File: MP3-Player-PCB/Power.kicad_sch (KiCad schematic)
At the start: 3 parts, among them J301 Conn_01x02_Socket, U301 BQ24259, U302 TLV73333PDBV

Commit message: Started power schematic
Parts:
- added C201, C202: 100n, symbol Device:C
- added C203, C204, C206, C207, C208, C209: 10u, symbol Device:C
- added C205: 47n, symbol Device:C
- added J202: USB_C_Receptacle_USB2.0_16P, symbol Connector:USB_C_Receptacle_USB2.0_16P
- added L201: L, symbol Device:L
- added R201: 0R, symbol Device:R
- added R202, R203: 5.1k, symbol Device:R
- added R204: R, symbol Device:R
- added U203: TLV73333PDBV, Package_TO_SOT_SMD:SOT-23-5, symbol Regulator_Linear:TLV73333PDBV
- added U204: USBLC6-2SC6, Package_TO_SOT_SMD:SOT-23-6, symbol Power_Protection:USBLC6-2SC6
- renumbered J301 to J201, U301 to U201, U302 to U202
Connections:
- net +VUSB_FILT: now reaches U201.1 (VBUS)
- net +VUSB_FILT: now also U201.24 (VBUS), C201.1, C203.1, R201.2
- net at U201.10 (ILIM): now also R204.1
- net GND: now reaches U201.17 (PGND)
- net GND: now also U201.18 (PGND), C201.2, C202.2, C203.2, C204.2, C206.2, C207.2, C208.2, C209.2, J202.A1 (GND), J202.A12 (GND), J202.B1 (GND), J202.B12 (GND), J202.S1 (SHIELD), R202.2, R203.2, R204.2
- net at U201.19 (SW): now also U201.20 (SW), C205.2, L201.1
- net at U201.21 (BTST): now also C205.1
- net at U201.23 (PMID): now also C204.1
- new net +VSYS: C206.1, C207.1, C208.1, C209.1, L201.2
- new net +VUSB: C202.1, J202.A4 (VBUS), J202.A9 (VBUS), J202.B4 (VBUS), J202.B9 (VBUS), R201.1
- new net USB_CON_CC1: J202.A5 (CC1), R202.1
- new net USB_CON_CC2: J202.B5 (CC2), R203.1
- new net USB_CON_D+: J202.A6 (D+), J202.B6 (D+), U204.3 (I/O2)
- new net USB_CON_D-: J202.A7 (D-), J202.B7 (D-), U204.1 (I/O1)
- new net USB_MCU_D+: U204.4 (I/O2)
- new net USB_MCU_D-: U204.6 (I/O1)
- no-connect marks 0 -> 2
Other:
- moved on the sheet: J201, U201, U202

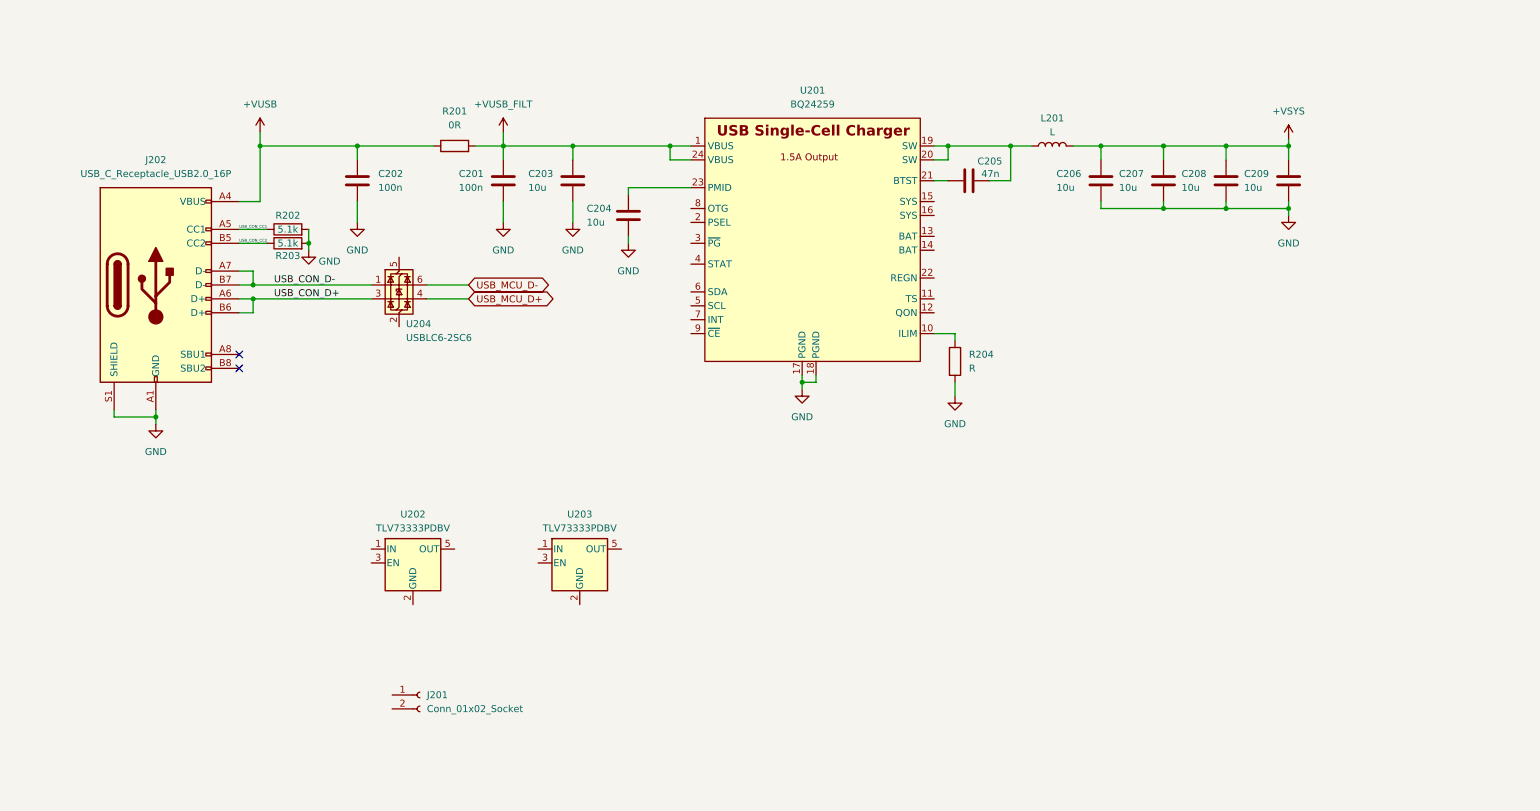
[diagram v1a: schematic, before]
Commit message: Adding i2c connections to charger ic as well as ntc safety logic
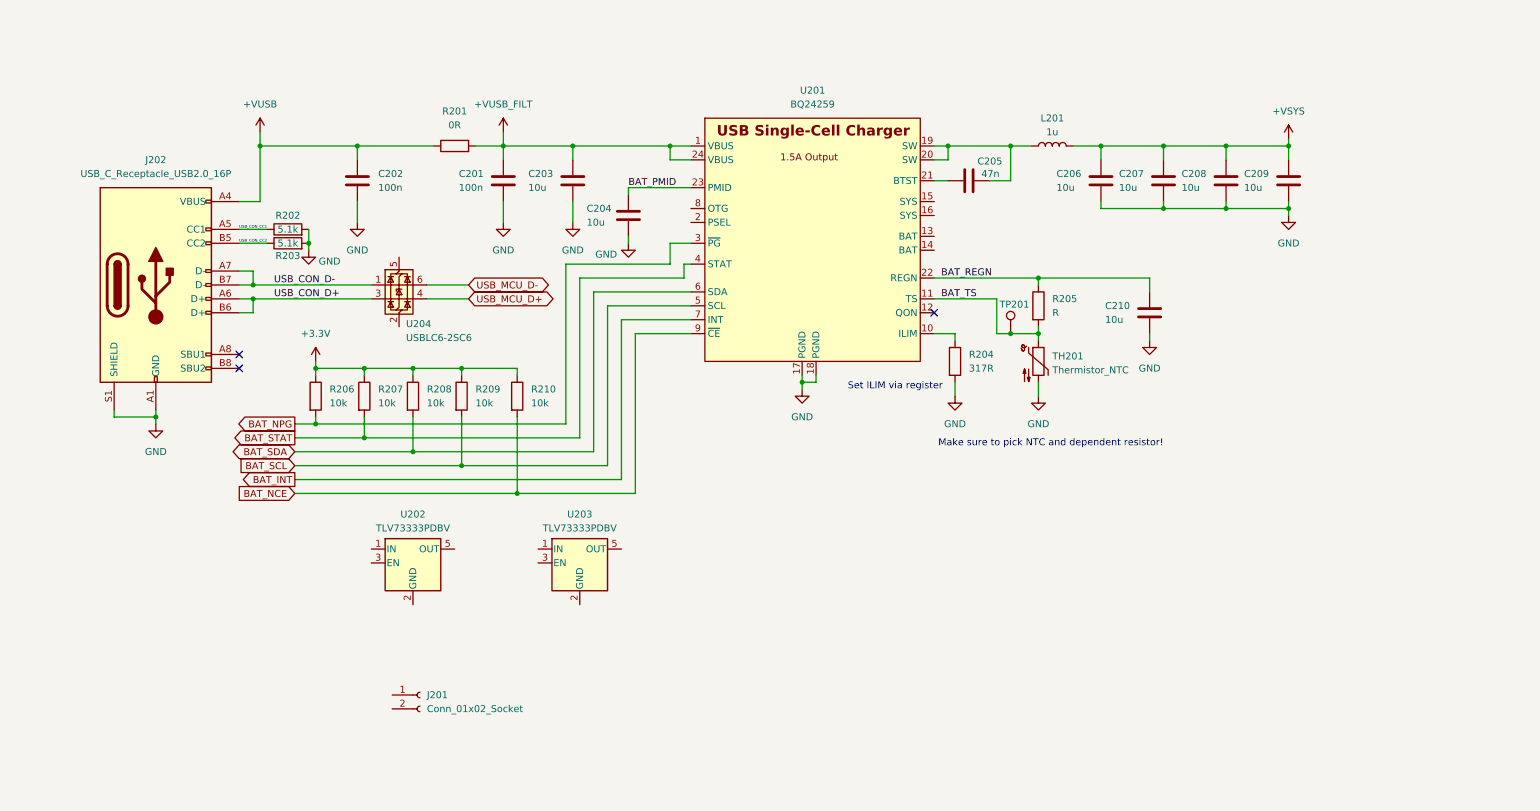
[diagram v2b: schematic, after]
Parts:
- added C210: 10u, symbol Device:C
- added R205: R, symbol Device:R
- added R206, R207, R208, R209, R210: 10k, symbol Device:R
- added TH201: Thermistor_NTC, symbol Device:Thermistor_NTC
- added TP201: TestPoint, symbol Connector:TestPoint
- L201: value L -> 1u
- R204: value R -> 317R
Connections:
- net GND: now also C210.2, TH201.2
- net BAT_PMID: now reaches C204.1, U201.23 (PMID)
- net BAT_TS: now reaches U201.11 (TS)
- net BAT_TS: now also R205.2, TH201.1, TP201.1
- net BAT_REGN: now reaches U201.22 (REGN)
- net BAT_REGN: now also C210.1, R205.1
- net BAT_NPG: now reaches U201.3 (~{PG})
- net BAT_NPG: now also R206.2
- net BAT_STAT: now reaches U201.4 (STAT)
- net BAT_STAT: now also R207.2
- net BAT_SCL: now reaches U201.5 (SCL)
- net BAT_SCL: now also R209.2
- net BAT_SDA: now reaches U201.6 (SDA)
- net BAT_SDA: now also R208.2
- net BAT_INT: now reaches U201.7 (INT)
- net BAT_NCE: now reaches U201.9 (~{CE})
- net BAT_NCE: now also R210.2
- new net +3.3V: R206.1, R207.1, R208.1, R209.1, R210.1
- no-connect marks 2 -> 3
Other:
- note added: "Make sure to pick NTC and dependent resistor!"
- note added: "Set ILIM via register"

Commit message: Added charger IC schematic circuitry
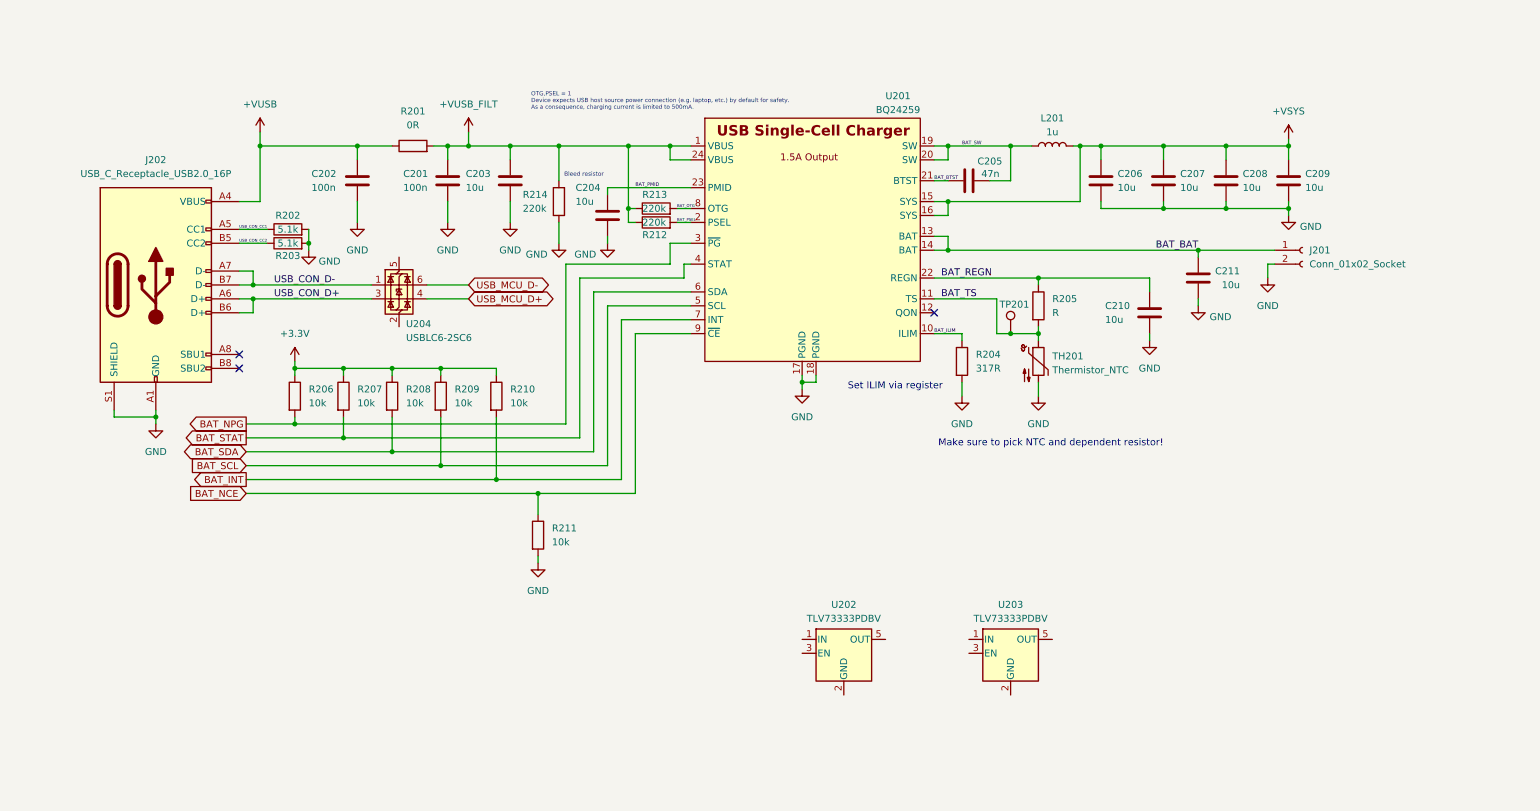
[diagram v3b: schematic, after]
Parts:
- added C211: 10u, symbol Device:C
- added R211: 10k, symbol Device:R
- added R212, R213, R214: 220k, symbol Device:R
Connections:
- net +VSYS: now also U201.15 (SYS), U201.16 (SYS)
- net +VUSB_FILT: now also R212.1, R213.1, R214.2
- net BAT_INT: now also R210.2
- net BAT_NCE: now also R211.1; no longer R210.2
- net GND: now also J201.2 (Pin_2), C211.2, R211.2, R214.1
- net BAT_BAT: now reaches J201.1 (Pin_1)
- net BAT_BAT: now also U201.13 (BAT), U201.14 (BAT), C211.1
- net BAT_ILIM: now reaches R204.1, U201.10 (ILIM)
- net BAT_SW: now reaches C205.2, L201.1, U201.19 (SW), U201.20 (SW)
- net BAT_PSEL: now reaches U201.2 (PSEL)
- net BAT_PSEL: now also R212.2
- net BAT_BTST: now reaches C205.1, U201.21 (BTST)
- net BAT_OTG: now reaches U201.8 (OTG)
- net BAT_OTG: now also R213.2
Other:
- note added: "Bleed resistor"
- note added: "OTG,PSEL = 1 Device expects USB host source power connection (e.g. laptop, etc.) by default for safety. As a consequence, charging current is limited to 500mA."
- moved on the sheet: C201, C203, C204, J201, R201, R204, R206, R207, R208, R209, R210, U202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

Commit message: Added new LDO (TPS7A20) schematic symbol and wired it up on power page for both analog and digital supplies
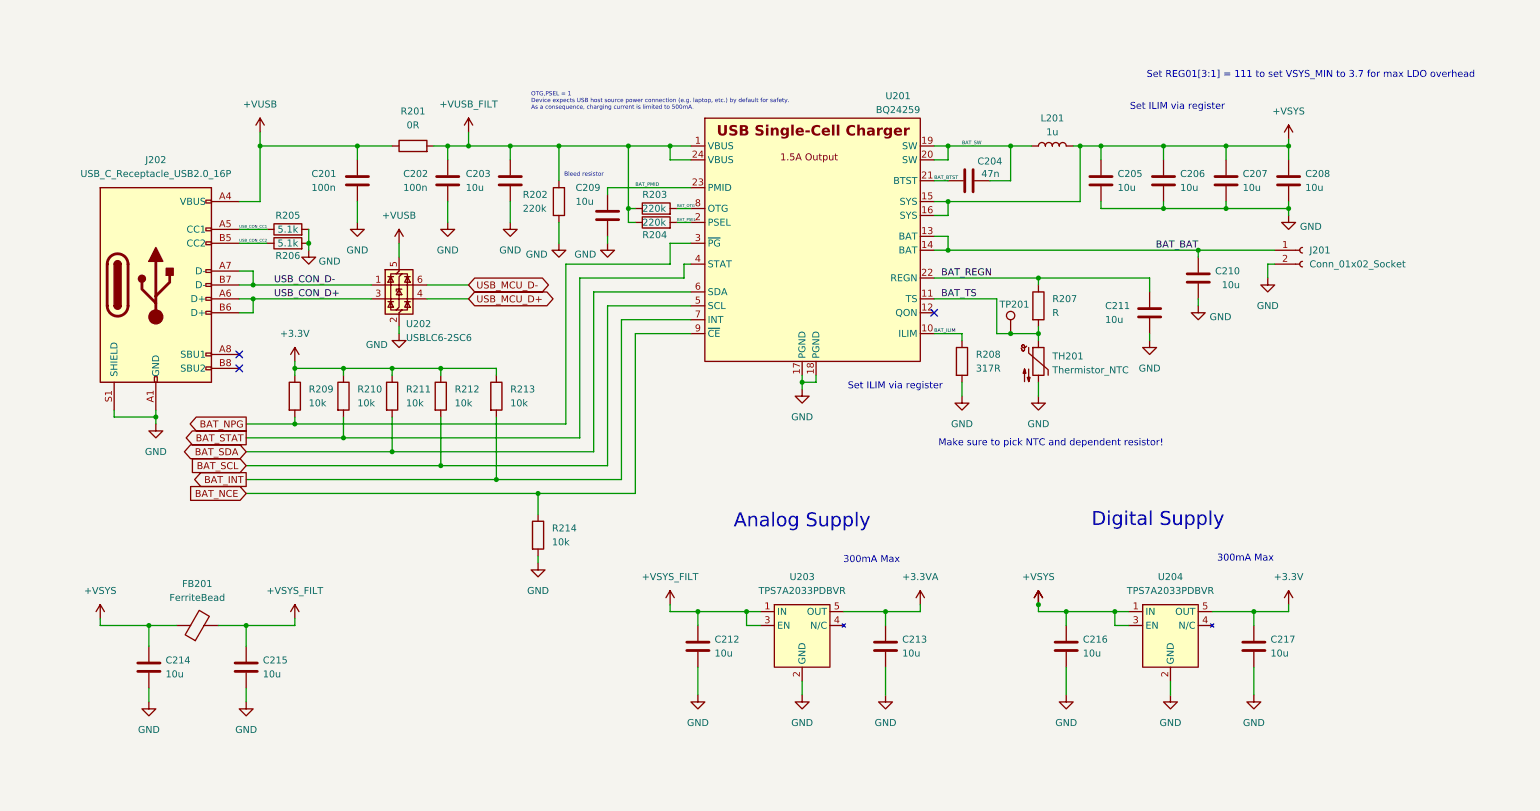
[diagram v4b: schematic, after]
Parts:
- removed U202, U203: TLV73333PDBV, Package_TO_SOT_SMD:SOT-23-5, symbol Regulator_Linear:TLV73333PDBV
- added C212, C213, C214, C215, C216, C217: 10u, symbol Device:C
- added FB201: FerriteBead, symbol Device:FerriteBead
- added U203, U204: TPS7A2033PDBVR, symbol MP3-Player_Symbol_Libraries:TPS7A2033PDBVR
- renumbered C202 to C201, C201 to C202, C205 to C204, C206 to C205, C207 to C206, C208 to C207, C209 to C208, C204 to C209, C211 to C210, C210 to C211, R214 to R202, R213 to R203, R212 to R204, R202 to R205, R203 to R206, R205 to R207, R204 to R208, R206 to R209, R207 to R210, R208 to R211, R209 to R212, R210 to R213, R211 to R214, U204 to U202
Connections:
- net +3.3V: now also C217.1, U204.5 (OUT)
- net +VSYS: now also C212.1, C214.1, C215.1, C216.1, FB201.1, FB201.2, U203.1 (IN), U203.3 (EN), U204.1 (IN), U204.3 (EN)
- net +VUSB: now also U202.5 (VBUS)
- net GND: now also U202.2 (GND), C212.2, C213.2, C214.2, C215.2, C216.2, C217.2, U203.2 (GND), U204.2 (GND)
- new net +3.3VA: C213.1, U203.5 (OUT)
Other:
- note added: "300mA Max"
- note added: "Analog Supply"
- note added: "Digital Supply"
- note added: "Set REG01[3:1] = 111 to set VSYS_MIN to 3.7 for max LDO overhead"

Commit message: Added addressable LED circuitry
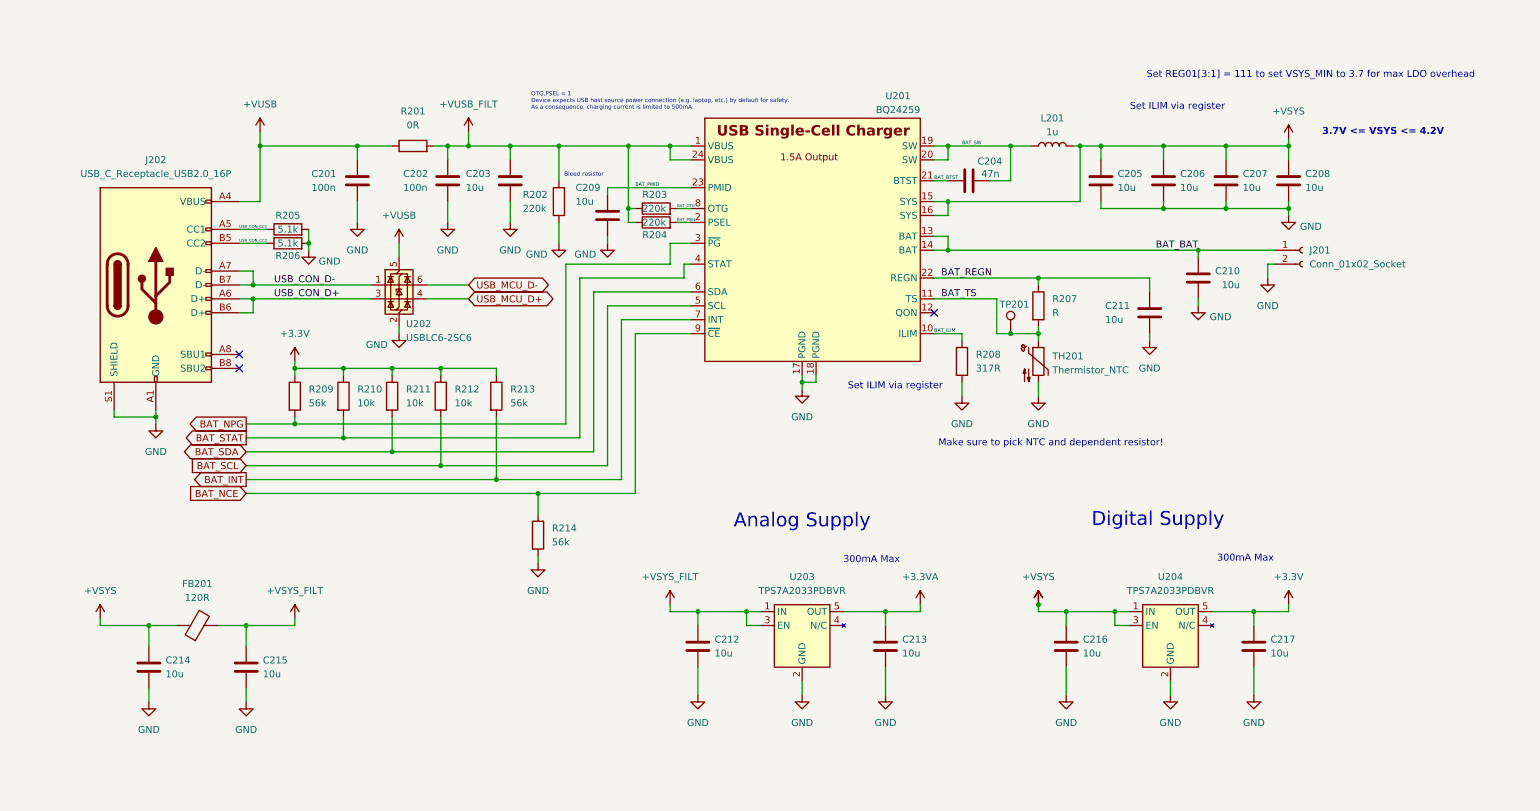
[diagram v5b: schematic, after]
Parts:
- FB201: value FerriteBead -> 120R
- R209, R213, R214: value 10k -> 56k
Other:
- note added: "3.7V <= VSYS <= 4.2V"
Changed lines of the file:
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@@
 		)
 	)
+	(text "3.7V <= VSYS <= 4.2V"
+		(exclude_from_sim no)
+		(at 263.652 38.1 0)
+		(effects
+			(font
+				(size 1.27 1.27)
+				(thickness 0.254)
+				(bold yes)
+			)
+		)
+	)
 	(text "Set REG01[3:1] = 111 to set VSYS_MIN to 3.7 for max LDO overhead"
 		(exclude_from_sim no)
@@
 			)
 		)
-		(property "Value" "FerriteBead"
+		(property "Value" "120R"
 			(at 46.9392 123.19 90)
 			(effects
@@
 			)
 		)
-		(property "Value" "10k"
+		(property "Value" "56k"
 			(at 104.14 87.6299 0)
 			(effects
@@
 			)
 		)
-		(property "Value" "10k"
+		(property "Value" "56k"
 			(at 67.31 87.6299 0)
 			(effects
@@
 			)
 		)
-		(property "Value" "10k"
+		(property "Value" "56k"
 			(at 111.76 113.0299 0)
 			(effects
